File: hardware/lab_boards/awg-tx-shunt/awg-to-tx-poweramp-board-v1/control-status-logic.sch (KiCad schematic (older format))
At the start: 9 parts

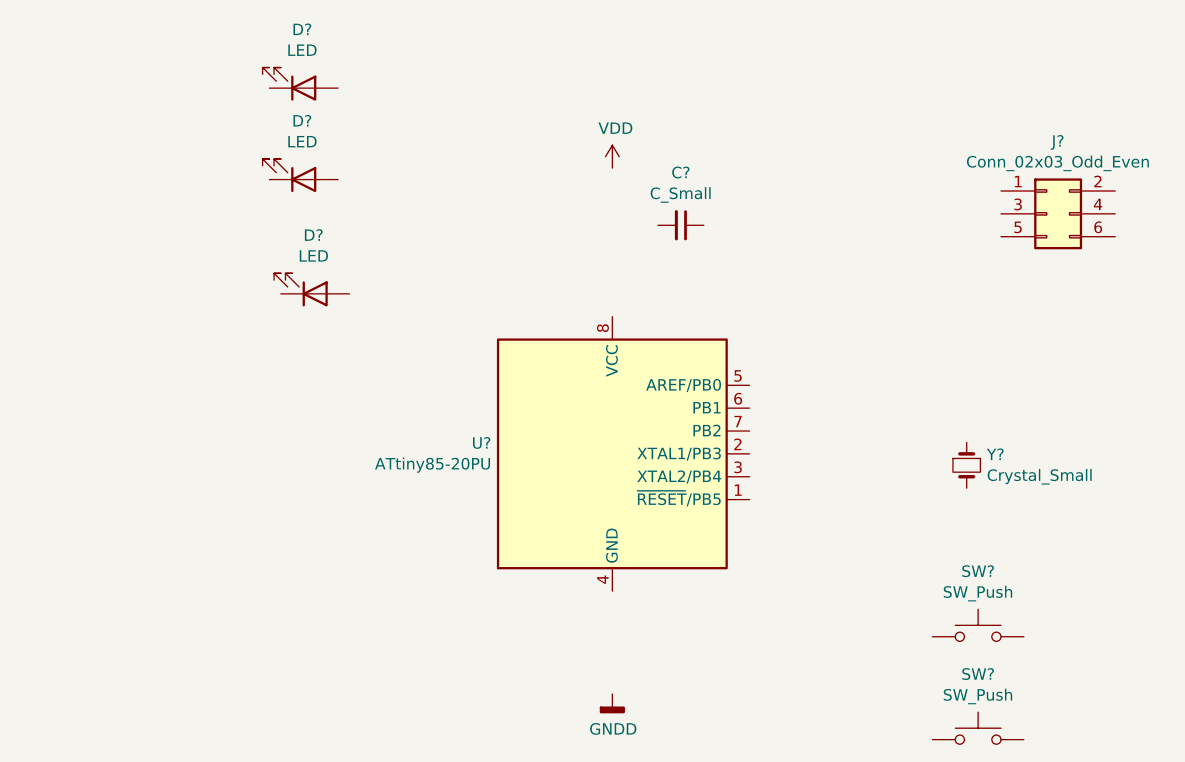
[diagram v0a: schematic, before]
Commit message: Added some TTL logic controls for interfacing with either the USB DAQ or a custom MCU solution.
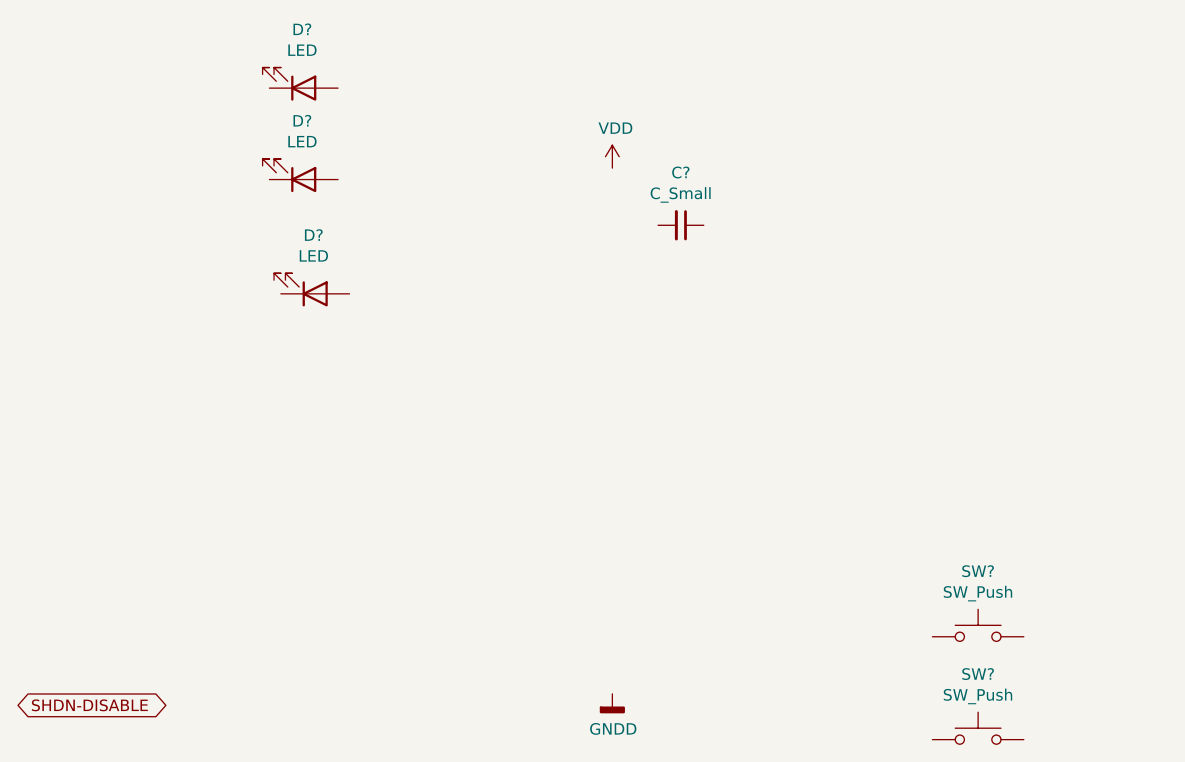
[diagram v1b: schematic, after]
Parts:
- removed J?: Conn_02x03_Odd_Even, symbol Connector_Generic:Conn_02x03_Odd_Even
- removed U?: ATtiny85-20PU, Package_DIP:DIP-8_W7.62mm, symbol MCU_Microchip_ATtiny:ATtiny85-20PU
- removed Y?: Crystal_Small, symbol Device:Crystal_Small
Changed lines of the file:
@@
 $EndDescr
-$Comp
-L MCU_Microchip_ATtiny:ATtiny85-20PU U?
-U 1 1 5F98B5E3
-P 5600 3150
-F 0 "U?" H 5071 3196 50  0000 R CNN
-F 1 "ATtiny85-20PU" H 5071 3105 50  0000 R CNN
-F 2 "Package_DIP:DIP-8_W7.62mm" H 5600 3150 50  0001 C CIN
-F 3 "http://ww1.microchip.com/downloads/en/DeviceDoc/atmel-2586-avr-8-bit-microcontroller-attiny25-attiny45-attiny85_datasheet.pdf" H 5600 3150 50  0001 C CNN
-	1    5600 3150
-	1    0    0    -1
-$EndComp
-$Comp
-L Device:Crystal_Small Y?
-U 1 1 5F98C2EB
-P 7150 3200
-F 0 "Y?" V 7104 3288 50  0000 L CNN
-F 1 "Crystal_Small" V 7195 3288 50  0000 L CNN
-F 2 "" H 7150 3200 50  0001 C CNN
-F 3 "~" H 7150 3200 50  0001 C CNN
-	1    7150 3200
-	0    1    1    0
-$EndComp
 $Comp
 L Device:C_Small C?
@@
 	1    5900 2150
 	0    1    1    0
-$EndComp
-$Comp
-L Connector_Generic:Conn_02x03_Odd_Even J?
-U 1 1 5F98F62C
-P 7500 2100
-F 0 "J?" H 7550 2417 50  0000 C CNN
-F 1 "Conn_02x03_Odd_Even" H 7550 2326 50  0000 C CNN
-F 2 "" H 7500 2100 50  0001 C CNN
-F 3 "~" H 7500 2100 50  0001 C CNN
-	1    7500 2100
-	1    0    0    -1
 $EndComp
 $Comp
@@
 	1    0    0    1
 $EndComp
+Text GLabel 3000 4250 2    50   BiDi ~ 0
+SHDN-DISABLE
 $EndSCHEMATC
